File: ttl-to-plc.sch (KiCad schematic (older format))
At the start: 30 parts, among them J1 Screw_Terminal_01x04, J2 Conn_02x04_Odd_Even, Q1 BC546, Q2 BC546, Q3 BC327, Q4 BC327, Q5 BC546, Q6 BC546, Q7 BC327, Q8 BC327

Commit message: ttl->plc: replaced BC546 with 2N7002 to comply with typical logic levels voltages in Arduino
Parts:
- removed Q1, Q2, Q5, Q6: BC546, Package_TO_SOT_SMD:TSOT-23_HandSoldering, symbol Transistor_BJT:BC546
- added Q? (x4): 2N7002, Package_TO_SOT_SMD:SOT-23, symbol Transistor_FET:2N7002
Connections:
- net labels added: +24V
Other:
- moved on the sheet: Q3, Q4, Q8, R1, R10, R12, R14, R16, R18, R2, R20, R3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

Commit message: Reorganized everything to use hierarchical sheets in KiCAD. Moved power supply section for motor driver into separate sheet. Moved connectors into top-level sheet
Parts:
- removed J1: Screw_Terminal_01x04, TerminalBlock_RND:TerminalBlock_RND_205-00003_1x04_P5.00mm_Horizontal, symbol Connector:Screw_Terminal_01x04
- removed J2: Conn_02x04_Odd_Even, mylib:DG500B-5.0-4P14, symbol Connector_Generic:Conn_02x04_Odd_Even
- removed Q? (x3): 2N7002, Package_TO_SOT_SMD:SOT-23, symbol Transistor_FET:2N7002
- added Q2, Q5, Q6: 2N7002, Package_TO_SOT_SMD:SOT-23, symbol Transistor_FET:2N7002
- gave numbers to parts that had none: 1
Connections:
- net labels added: 24V, IN1, IN2, IN3, IN4, OUT1, OUT2, OUT3, OUT4
- net labels removed: +24V, I10, I11, I12, I13, O10+, O10-, O11+, O11-, O12+, O12-, O13+, O13-, VCC
- wire segments 106 -> 92
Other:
- moved on the sheet: Q1, Q3, R1, R3, R5, R7, R9

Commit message: Added power supply section to PCB. Added missing components footprints.
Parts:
- Q1, Q2, Q5, Q6: footprint Package_TO_SOT_SMD:SOT-23 -> Package_TO_SOT_SMD:SOT-23_Handsoldering
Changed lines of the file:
@@
 Connection ~ 4150 3050
 $Comp
-L power:GND #PWR03
+L power:GND #PWR01
 U 1 1 5BD24757
 P 4150 3150
-F 0 "#PWR03" H 4150 2900 50  0001 C CNN
+F 0 "#PWR01" H 4150 2900 50  0001 C CNN
 F 1 "GND" H 4155 2977 50  0000 C CNN
 F 2 "" H 4150 3150 50  0001 C CNN
@@
 F 0 "Q1" H 4655 2596 50  0000 L CNN
 F 1 "2N7002" H 4655 2505 50  0000 L CNN
-F 2 "Package_TO_SOT_SMD:SOT-23" H 4650 2475 50  0001 L CIN
+F 2 "Package_TO_SOT_SMD:SOT-23_Handsoldering" H 4650 2475 50  0001 L CIN
 F 3 "https://www.fairchildsemi.com/datasheets/2N/2N7002.pdf" H 4450 2550 50  0001 L CNN
 	1    4450 2550
@@
 Connection ~ 7000 3050
 $Comp
-L power:GND #PWR06
+L power:GND #PWR03
 U 1 1 5C04156B
 P 7000 3150
-F 0 "#PWR06" H 7000 2900 50  0001 C CNN
+F 0 "#PWR03" H 7000 2900 50  0001 C CNN
 F 1 "GND" H 7005 2977 50  0000 C CNN
 F 2 "" H 7000 3150 50  0001 C CNN
@@
 F 0 "Q5" H 7505 2596 50  0000 L CNN
 F 1 "2N7002" H 7505 2505 50  0000 L CNN
-F 2 "Package_TO_SOT_SMD:SOT-23" H 7500 2475 50  0001 L CIN
+F 2 "Package_TO_SOT_SMD:SOT-23_Handsoldering" H 7500 2475 50  0001 L CIN
 F 3 "https://www.fairchildsemi.com/datasheets/2N/2N7002.pdf" H 7300 2550 50  0001 L CNN
 	1    7300 2550
@@
 Connection ~ 4150 5100
 $Comp
-L power:GND #PWR04
+L power:GND #PWR02
 U 1 1 5C042086
 P 4150 5200
-F 0 "#PWR04" H 4150 4950 50  0001 C CNN
+F 0 "#PWR02" H 4150 4950 50  0001 C CNN
 F 1 "GND" H 4155 5027 50  0000 C CNN
 F 2 "" H 4150 5200 50  0001 C CNN
@@
 F 0 "Q2" H 4655 4646 50  0000 L CNN
 F 1 "2N7002" H 4655 4555 50  0000 L CNN
-F 2 "Package_TO_SOT_SMD:SOT-23" H 4650 4525 50  0001 L CIN
+F 2 "Package_TO_SOT_SMD:SOT-23_Handsoldering" H 4650 4525 50  0001 L CIN
 F 3 "https://www.fairchildsemi.com/datasheets/2N/2N7002.pdf" H 4450 4600 50  0001 L CNN
 	1    4450 4600
@@
 Connection ~ 7000 5100
 $Comp
-L power:GND #PWR07
+L power:GND #PWR04
 U 1 1 5C0439B1
 P 7000 5200
-F 0 "#PWR07" H 7000 4950 50  0001 C CNN
+F 0 "#PWR04" H 7000 4950 50  0001 C CNN
 F 1 "GND" H 7005 5027 50  0000 C CNN
 F 2 "" H 7000 5200 50  0001 C CNN
@@
 F 0 "Q6" H 7505 4646 50  0000 L CNN
 F 1 "2N7002" H 7505 4555 50  0000 L CNN
-F 2 "Package_TO_SOT_SMD:SOT-23" H 7500 4525 50  0001 L CIN
+F 2 "Package_TO_SOT_SMD:SOT-23_Handsoldering" H 7500 4525 50  0001 L CIN
 F 3 "https://www.fairchildsemi.com/datasheets/2N/2N7002.pdf" H 7300 4600 50  0001 L CNN
 	1    7300 4600

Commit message: Further work at PCB
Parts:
- R1, R10, R11, R12, R13, R14, R17, R18, R19, R2, R20, R3, R4, R7, R8, R9: footprint Resistor_SMD:R_0805_2012Metric_Pad1.15x1.40mm_HandSolder -> Resistor_SMD:R_0603_1608Metric_Pad1.05x0.95mm_HandSolder
- R15, R16, R5, R6: footprint Resistor_SMD:R_1206_3216Metric_Pad1.42x1.75mm_HandSolder -> Resistor_SMD:R_0805_2012Metric_Pad1.15x1.40mm_HandSolder
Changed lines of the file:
@@
 F 0 "R9" H 5520 2846 50  0000 L CNN
 F 1 "100k" H 5520 2755 50  0000 L CNN
-F 2 "Resistor_SMD:R_0805_2012Metric_Pad1.15x1.40mm_HandSolder" V 5380 2800 50  0001 C CNN
+F 2 "Resistor_SMD:R_0603_1608Metric_Pad1.05x0.95mm_HandSolder" V 5380 2800 50  0001 C CNN
 F 3 "~" H 5450 2800 50  0001 C CNN
 	1    5450 2800
@@
 F 0 "R7" H 4980 1954 50  0000 R CNN
 F 1 "100k" H 4980 2045 50  0000 R CNN
-F 2 "Resistor_SMD:R_0805_2012Metric_Pad1.15x1.40mm_HandSolder" V 4980 2000 50  0001 C CNN
+F 2 "Resistor_SMD:R_0603_1608Metric_Pad1.05x0.95mm_HandSolder" V 4980 2000 50  0001 C CNN
 F 3 "~" H 5050 2000 50  0001 C CNN
 	1    5050 2000
@@
 F 0 "R5" V 5007 2250 50  0000 C CNN
 F 1 "10k" V 4916 2250 50  0000 C CNN
-F 2 "Resistor_SMD:R_1206_3216Metric_Pad1.42x1.75mm_HandSolder" V 4730 2250 50  0001 C CNN
+F 2 "Resistor_SMD:R_0805_2012Metric_Pad1.15x1.40mm_HandSolder" V 4730 2250 50  0001 C CNN
 F 3 "~" H 4800 2250 50  0001 C CNN
 	1    4800 2250
@@
 F 0 "R3" H 4220 2846 50  0000 L CNN
 F 1 "47k" H 4220 2755 50  0000 L CNN
-F 2 "Resistor_SMD:R_0805_2012Metric_Pad1.15x1.40mm_HandSolder" V 4080 2800 50  0001 C CNN
+F 2 "Resistor_SMD:R_0603_1608Metric_Pad1.05x0.95mm_HandSolder" V 4080 2800 50  0001 C CNN
 F 3 "~" H 4150 2800 50  0001 C CNN
 	1    4150 2800
@@
 F 0 "R1" V 3693 2550 50  0000 C CNN
 F 1 "4.7k" V 3784 2550 50  0000 C CNN
-F 2 "Resistor_SMD:R_0805_2012Metric_Pad1.15x1.40mm_HandSolder" V 3830 2550 50  0001 C CNN
+F 2 "Resistor_SMD:R_0603_1608Metric_Pad1.05x0.95mm_HandSolder" V 3830 2550 50  0001 C CNN
 F 3 "~" H 3900 2550 50  0001 C CNN
 	1    3900 2550
@@
 F 0 "R19" H 8370 2846 50  0000 L CNN
 F 1 "100k" H 8370 2755 50  0000 L CNN
-F 2 "Resistor_SMD:R_0805_2012Metric_Pad1.15x1.40mm_HandSolder" V 8230 2800 50  0001 C CNN
+F 2 "Resistor_SMD:R_0603_1608Metric_Pad1.05x0.95mm_HandSolder" V 8230 2800 50  0001 C CNN
 F 3 "~" H 8300 2800 50  0001 C CNN
 	1    8300 2800
@@
 F 0 "R17" H 7830 1954 50  0000 R CNN
 F 1 "100k" H 7830 2045 50  0000 R CNN
-F 2 "Resistor_SMD:R_0805_2012Metric_Pad1.15x1.40mm_HandSolder" V 7830 2000 50  0001 C CNN
+F 2 "Resistor_SMD:R_0603_1608Metric_Pad1.05x0.95mm_HandSolder" V 7830 2000 50  0001 C CNN
 F 3 "~" H 7900 2000 50  0001 C CNN
 	1    7900 2000
@@
 F 0 "R15" V 7857 2250 50  0000 C CNN
 F 1 "10k" V 7766 2250 50  0000 C CNN
-F 2 "Resistor_SMD:R_1206_3216Metric_Pad1.42x1.75mm_HandSolder" V 7580 2250 50  0001 C CNN
+F 2 "Resistor_SMD:R_0805_2012Metric_Pad1.15x1.40mm_HandSolder" V 7580 2250 50  0001 C CNN
 F 3 "~" H 7650 2250 50  0001 C CNN
 	1    7650 2250
@@
 F 0 "R13" H 7070 2846 50  0000 L CNN
 F 1 "47k" H 7070 2755 50  0000 L CNN
-F 2 "Resistor_SMD:R_0805_2012Metric_Pad1.15x1.40mm_HandSolder" V 6930 2800 50  0001 C CNN
+F 2 "Resistor_SMD:R_0603_1608Metric_Pad1.05x0.95mm_HandSolder" V 6930 2800 50  0001 C CNN
 F 3 "~" H 7000 2800 50  0001 C CNN
 	1    7000 2800
@@
 F 0 "R11" V 6543 2550 50  0000 C CNN
 F 1 "4.7k" V 6634 2550 50  0000 C CNN
-F 2 "Resistor_SMD:R_0805_2012Metric_Pad1.15x1.40mm_HandSolder" V 6680 2550 50  0001 C CNN
+F 2 "Resistor_SMD:R_0603_1608Metric_Pad1.05x0.95mm_HandSolder" V 6680 2550 50  0001 C CNN
 F 3 "~" H 6750 2550 50  0001 C CNN
 	1    6750 2550
@@
 F 0 "R10" H 5520 4896 50  0000 L CNN
 F 1 "100k" H 5520 4805 50  0000 L CNN
-F 2 "Resistor_SMD:R_0805_2012Metric_Pad1.15x1.40mm_HandSolder" V 5380 4850 50  0001 C CNN
+F 2 "Resistor_SMD:R_0603_1608Metric_Pad1.05x0.95mm_HandSolder" V 5380 4850 50  0001 C CNN
 F 3 "~" H 5450 4850 50  0001 C CNN
 	1    5450 4850
@@
 F 0 "R8" H 4980 4004 50  0000 R CNN
 F 1 "100k" H 4980 4095 50  0000 R CNN
-F 2 "Resistor_SMD:R_0805_2012Metric_Pad1.15x1.40mm_HandSolder" V 4980 4050 50  0001 C CNN
+F 2 "Resistor_SMD:R_0603_1608Metric_Pad1.05x0.95mm_HandSolder" V 4980 4050 50  0001 C CNN
 F 3 "~" H 5050 4050 50  0001 C CNN
 	1    5050 4050
@@
 F 0 "R6" V 5007 4300 50  0000 C CNN
 F 1 "10k" V 4916 4300 50  0000 C CNN
-F 2 "Resistor_SMD:R_1206_3216Metric_Pad1.42x1.75mm_HandSolder" V 4730 4300 50  0001 C CNN
+F 2 "Resistor_SMD:R_0805_2012Metric_Pad1.15x1.40mm_HandSolder" V 4730 4300 50  0001 C CNN
 F 3 "~" H 4800 4300 50  0001 C CNN
 	1    4800 4300
@@
 F 0 "R4" H 4220 4896 50  0000 L CNN
 F 1 "47k" H 4220 4805 50  0000 L CNN
-F 2 "Resistor_SMD:R_0805_2012Metric_Pad1.15x1.40mm_HandSolder" V 4080 4850 50  0001 C CNN
+F 2 "Resistor_SMD:R_0603_1608Metric_Pad1.05x0.95mm_HandSolder" V 4080 4850 50  0001 C CNN
 F 3 "~" H 4150 4850 50  0001 C CNN
 	1    4150 4850
@@
 F 0 "R2" V 3693 4600 50  0000 C CNN
 F 1 "4.7k" V 3784 4600 50  0000 C CNN
-F 2 "Resistor_SMD:R_0805_2012Metric_Pad1.15x1.40mm_HandSolder" V 3830 4600 50  0001 C CNN
+F 2 "Resistor_SMD:R_0603_1608Metric_Pad1.05x0.95mm_HandSolder" V 3830 4600 50  0001 C CNN
 F 3 "~" H 3900 4600 50  0001 C CNN
 	1    3900 4600
@@
 F 0 "R20" H 8370 4896 50  0000 L CNN
 F 1 "100k" H 8370 4805 50  0000 L CNN
-F 2 "Resistor_SMD:R_0805_2012Metric_Pad1.15x1.40mm_HandSolder" V 8230 4850 50  0001 C CNN
+F 2 "Resistor_SMD:R_0603_1608Metric_Pad1.05x0.95mm_HandSolder" V 8230 4850 50  0001 C CNN
 F 3 "~" H 8300 4850 50  0001 C CNN
 	1    8300 4850
@@
 F 0 "R18" H 7830 4004 50  0000 R CNN
 F 1 "100k" H 7830 4095 50  0000 R CNN
-F 2 "Resistor_SMD:R_0805_2012Metric_Pad1.15x1.40mm_HandSolder" V 7830 4050 50  0001 C CNN
+F 2 "Resistor_SMD:R_0603_1608Metric_Pad1.05x0.95mm_HandSolder" V 7830 4050 50  0001 C CNN
 F 3 "~" H 7900 4050 50  0001 C CNN
 	1    7900 4050
@@
 F 0 "R16" V 7857 4300 50  0000 C CNN
 F 1 "10k" V 7766 4300 50  0000 C CNN
-F 2 "Resistor_SMD:R_1206_3216Metric_Pad1.42x1.75mm_HandSolder" V 7580 4300 50  0001 C CNN
+F 2 "Resistor_SMD:R_0805_2012Metric_Pad1.15x1.40mm_HandSolder" V 7580 4300 50  0001 C CNN
 F 3 "~" H 7650 4300 50  0001 C CNN
 	1    7650 4300
@@
 F 0 "R14" H 7070 4896 50  0000 L CNN
 F 1 "47k" H 7070 4805 50  0000 L CNN
-F 2 "Resistor_SMD:R_0805_2012Metric_Pad1.15x1.40mm_HandSolder" V 6930 4850 50  0001 C CNN
+F 2 "Resistor_SMD:R_0603_1608Metric_Pad1.05x0.95mm_HandSolder" V 6930 4850 50  0001 C CNN
 F 3 "~" H 7000 4850 50  0001 C CNN
 	1    7000 4850
@@
 F 0 "R12" V 6543 4600 50  0000 C CNN
 F 1 "4.7k" V 6634 4600 50  0000 C CNN
-F 2 "Resistor_SMD:R_0805_2012Metric_Pad1.15x1.40mm_HandSolder" V 6680 4600 50  0001 C CNN
+F 2 "Resistor_SMD:R_0603_1608Metric_Pad1.05x0.95mm_HandSolder" V 6680 4600 50  0001 C CNN
 F 3 "~" H 6750 4600 50  0001 C CNN
 	1    6750 4600

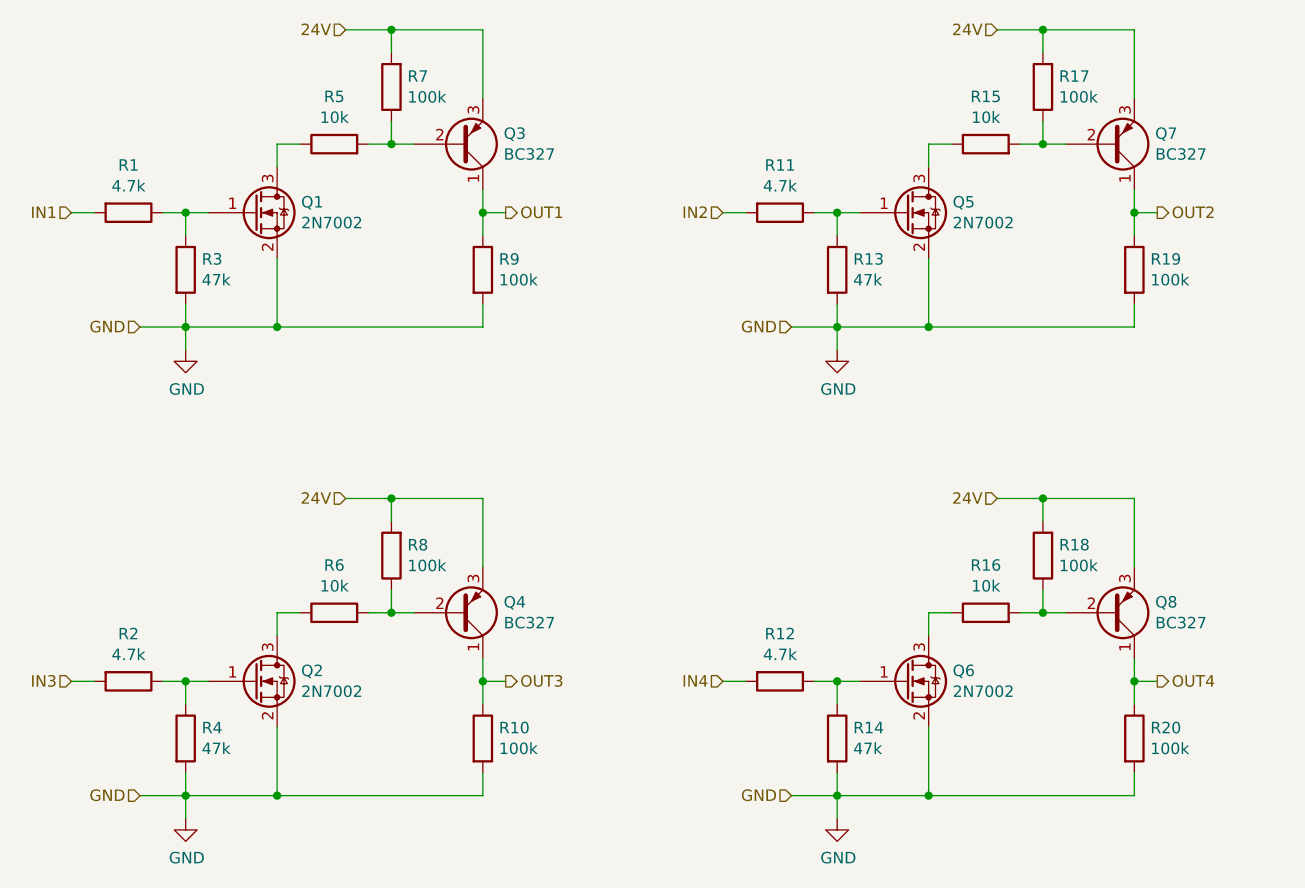
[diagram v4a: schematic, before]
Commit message: Changed Motor Controller to DRV8840, removed pre-motor power section. Replaced PNP transistors in logic level shifters with P-MOSFET units
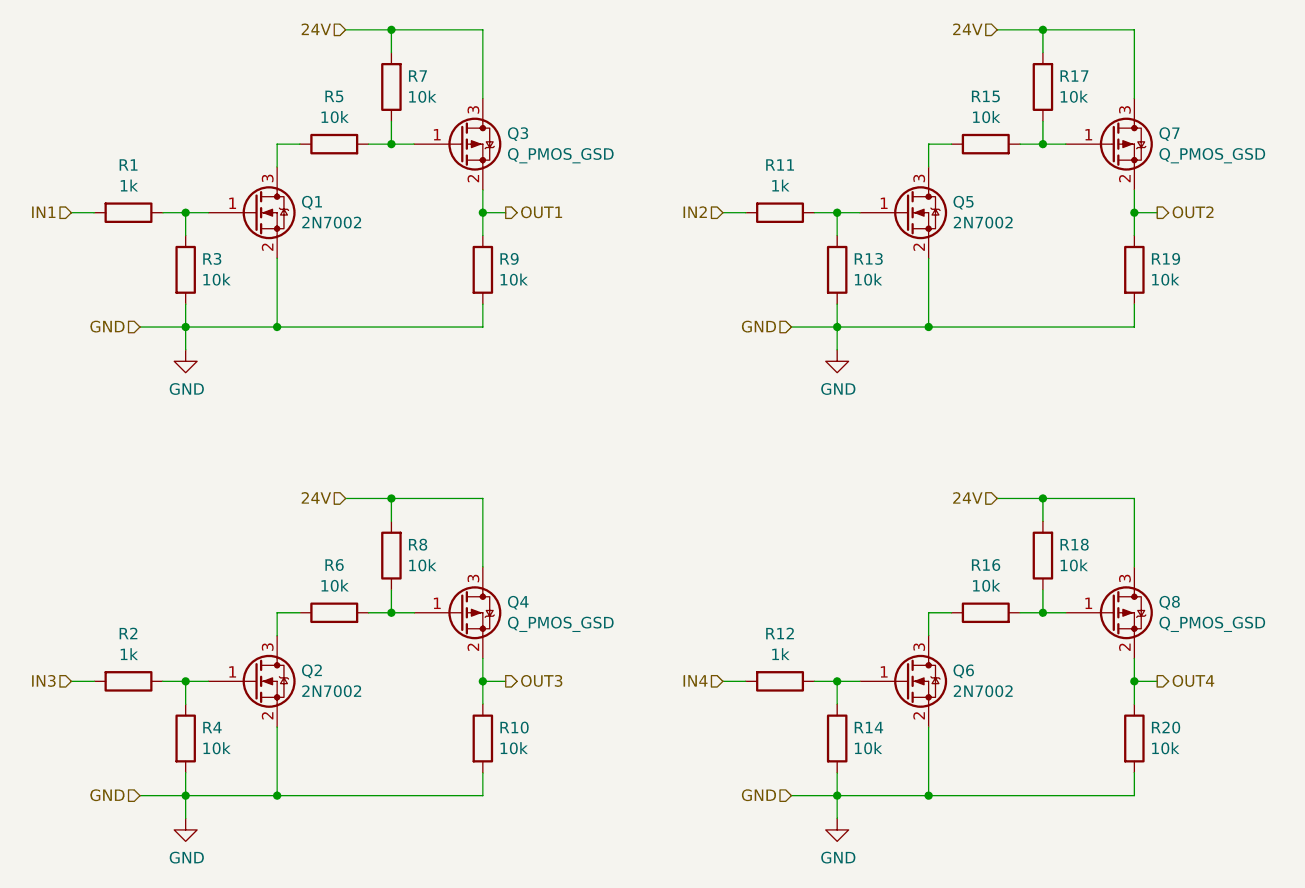
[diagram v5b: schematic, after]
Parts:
- removed Q3, Q4, Q7, Q8: BC327, Package_TO_SOT_THT:TO-92_Inline, symbol Transistor_BJT:BC327
- added Q3, Q4, Q7, Q8: Q_PMOS_GSD, Package_TO_SOT_SMD:SOT-23, symbol Device:Q_PMOS_GSD
- Q1, Q2, Q5, Q6: footprint Package_TO_SOT_SMD:SOT-23_Handsoldering -> Package_TO_SOT_SMD:SOT-23
- R1, R11, R12, R2: value 4.7k -> 1k; footprint Resistor_SMD:R_0603_1608Metric_Pad1.05x0.95mm_HandSolder -> Resistor_SMD:R_0603_1608Metric
- R10, R17, R18, R19, R20, R7, R8, R9: value 100k -> 10k; footprint Resistor_SMD:R_0603_1608Metric_Pad1.05x0.95mm_HandSolder -> Resistor_SMD:R_0603_1608Metric
- R13, R14, R3, R4: value 47k -> 10k; footprint Resistor_SMD:R_0603_1608Metric_Pad1.05x0.95mm_HandSolder -> Resistor_SMD:R_0603_1608Metric
- R15, R16, R5, R6: footprint Resistor_SMD:R_0805_2012Metric_Pad1.15x1.40mm_HandSolder -> Resistor_SMD:R_0603_1608Metric
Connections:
- net 24V: now also Q3.3 (D), Q4.3 (D), Q7.3 (D), Q8.3 (D)
- net OUT1: now also Q3.2 (S)
- net OUT2: now also Q7.2 (S)
- net OUT3: now also Q4.2 (S)
- net OUT4: now also Q8.2 (S)
- net at R5.2, R7.1: now also Q3.1 (G)
- net at R15.2, R17.1: now also Q7.1 (G)
- net at R6.2, R8.1: now also Q4.1 (G)
- net at R16.2, R18.1: now also Q8.1 (G)
